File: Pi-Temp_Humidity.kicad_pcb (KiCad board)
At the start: 2 copper layers, 27.9 x 15.2 mm, 12 parts, among them J1 Conn_01x05, J4 Conn_01x05, U1 HDC2010

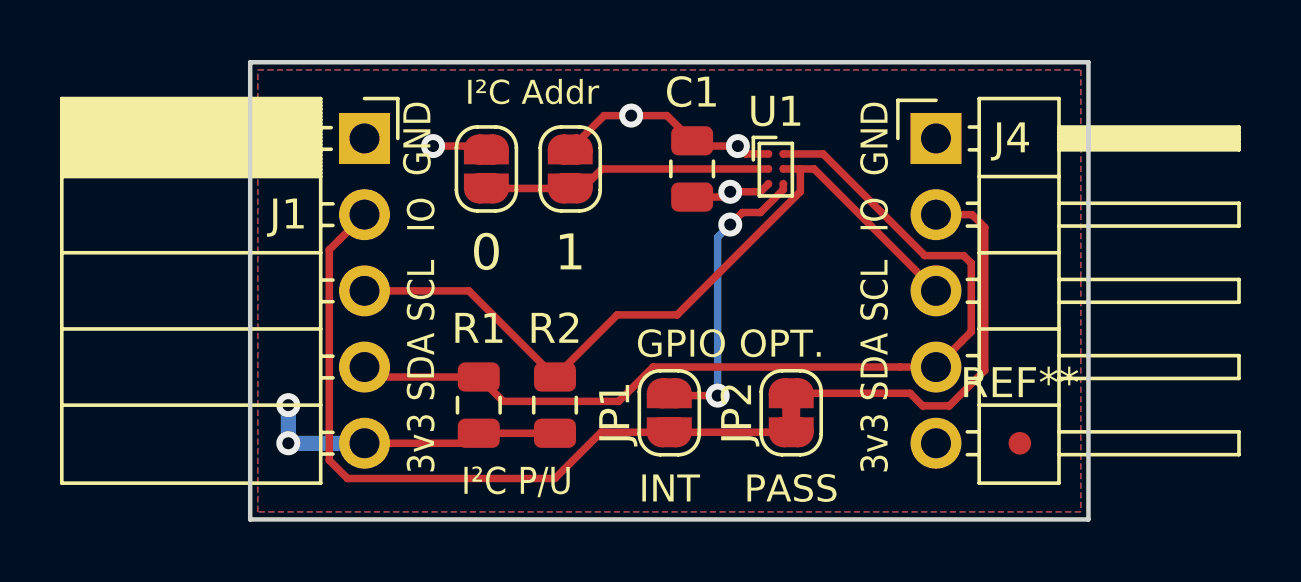
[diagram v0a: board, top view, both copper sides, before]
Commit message: Fixed footprint on HDC2010 & panelized
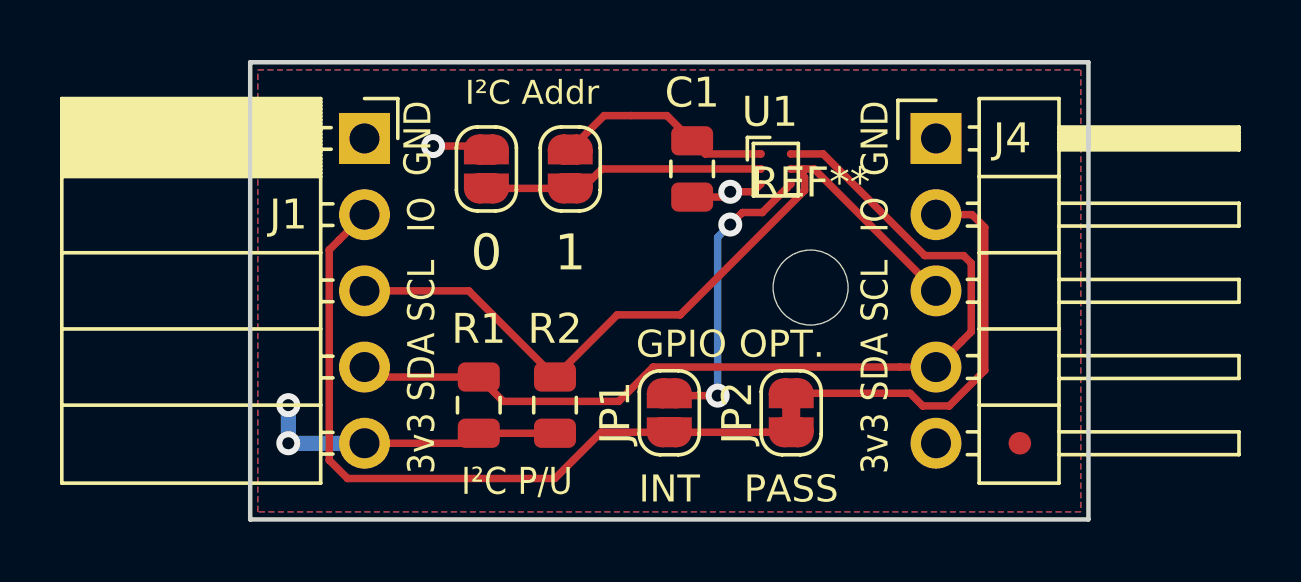
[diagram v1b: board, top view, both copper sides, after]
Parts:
- added REF**: MountingHole_2.5mm, MountingHole:MountingHole_2.5mm, F.Cu at (197.8, 86.2)
- U1: footprint Package_BGA:Texas_DSBGA-6_0.9x1.4mm_Layout2x3_P0.5mm -> Pi-Temp-Humidity:Texas_DSBGA-6
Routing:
- net VDD: track 18.1 -> 17.8 mm, vias 4 -> 2
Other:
- board text added: "1.8-3.6V ONLY"
- board text added: "I²C Temp/Humidity Rev B 20190210"
- board text removed: "I²C Temp/Humidity Rev A 201811110"
